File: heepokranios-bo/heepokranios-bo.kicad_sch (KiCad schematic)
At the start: 154 parts, among them J1 Conn_02x02_Odd_Even, J11 PGA_13x13, J14 Conn_02x03_Odd_Even, J15 Conn_02x08_Odd_Even, J16 Conn_02x03_Odd_Even, J17 Conn_02x03_Odd_Even, J2 Conn_02x02_Odd_Even, J21 Conn_01x02, J26 Conn_01x02, J27 Conn_01x02, J29 Conn_01x02, J3 Conn_02x03_Odd_Even, J30 Conn_01x02, J31 Conn_01x02, J32 Conn_01x02, J33 Conn_01x02, J34 Conn_01x02, J35 Conn_01x02, J36 Conn_01x02, J37 Conn_01x02, J38 Conn_01x02, J39 Conn_01x02, J4 Conn_02x03_Odd_Even, J40 Conn_01x02, J41 Conn_01x02, J42 Conn_01x02, J43 Conn_01x02, J48 Conn_01x02, J49 Conn_01x02, J5 Conn_02x03_Odd_Even, J6 Conn_02x04_Odd_Even, J8 Conn_02x03_Odd_Even, J9 Conn_02x02_Odd_Even, SW1 SW_Push, U1 BIWIN_DTS04GE_SMD

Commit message: Routing with extended PGA 13x13 socket
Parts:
- added R9: 330k, Resistor_SMD:R_0603_1608Metric, symbol Device:R_US
- R4: value 10k -> 330
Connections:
- net GND: now also R9.2
- net VREF_EN: now also R9.1
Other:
- note added: "(!) Pulled high from main"
- note added: "(!) VREF_EN added pull-down"
- note removed: "(!) VREF_EN add pull-down. This one is 1.2 V"
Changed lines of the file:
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@@
 	(rectangle
 		(start 105.41 266.7)
-		(end 153.67 290.83)
+		(end 153.67 292.1)
 		(stroke
 			(width 0)
@@
 	)
 	(rectangle
-		(start 105.41 292.1)
+		(start 105.41 293.37)
 		(end 153.67 316.23)
 		(stroke
@@
 	(rectangle
 		(start 160.02 106.68)
-		(end 187.96 128.27)
+		(end 200.66 128.27)
 		(stroke
 			(width 0)
@@
 	(text "VDD for the channel's LNAs"
 		(exclude_from_sim no)
-		(at 129.794 294.132 0)
+		(at 129.794 294.894 0)
 		(effects
 			(font
@@
 		)
 	)
-	(text "(!) VREF_EN add pull-down. This one is 1.2 V"
+	(text "(!) VREF_EN added pull-down"
 		(exclude_from_sim no)
-		(at 167.64 284.48 0)
+		(at 137.668 291.338 0)
 		(effects
 			(font
@@
 		)
 	)
+	(text " (!)\nPulled\nhigh from\nmain"
+		(exclude_from_sim no)
+		(at 194.056 116.586 0)
+		(effects
+			(font
+				(size 1.27 1.27)
+				(color 255 0 32 1)
+			)
+		)
+	)
 	(text "Reference for High (dirty) voltage"
 		(exclude_from_sim no)
@@
 	)
 	(junction
+		(at 186.69 121.92)
+		(diameter 0)
+		(color 0 0 0 0)
+	)
+	(junction
 		(at 436.88 217.17)
 		(diameter 0)
@@
 	)
 	(junction
-		(at 186.69 121.92)
-		(diameter 0)
-		(color 0 0 0 0)
-	)
-	(junction
 		(at 436.88 162.56)
 		(diameter 0)
@@
 	(wire
 		(pts
-			(xy 186.69 121.92) (xy 199.39 121.92)
+			(xy 186.69 121.92) (xy 204.47 121.92)
 		)
 		(stroke
@@
 	(wire
 		(pts
-			(xy 127 289.56) (xy 128.27 289.56)
+			(xy 127 289.56) (xy 137.16 289.56)
 		)
 		(stroke
@@
 	(wire
 		(pts
-			(xy 199.39 156.21) (xy 222.25 156.21)
+			(xy 204.47 156.21) (xy 222.25 156.21)
 		)
 		(stroke
@@
 	(wire
 		(pts
-			(xy 199.39 121.92) (xy 199.39 156.21)
+			(xy 144.78 289.56) (xy 147.32 289.56)
+		)
+		(stroke
+			(width 0)
+			(type default)
+		)
+	)
+	(wire
+		(pts
+			(xy 204.47 121.92) (xy 204.47 156.21)
 		)
 		(stroke
@@
 	(wire
 		(pts
+			(xy 316.23 156.21) (xy 306.07 156.21)
+		)
+		(stroke
+			(width 0)
+			(type default)
+		)
+	)
+	(wire
+		(pts
 			(xy 461.01 162.56) (xy 458.47 162.56)
 		)
@@
 	(wire
 		(pts
+			(xy 314.96 173.99) (xy 306.07 173.99)
+		)
+		(stroke
+			(width 0)
+			(type default)
+		)
+	)
+	(wire
+		(pts
 			(xy 130.81 314.96) (xy 132.08 314.96)
 		)
@@
 	)
 	(label "DMUX_0"
-		(at 306.07 156.21 0)
+		(at 316.23 156.21 0)
 		(effects
 			(font
@@
 	)
 	(label "DMUX_7"
-		(at 306.07 173.99 0)
+		(at 314.96 173.99 0)
 		(effects
 			(font
@@
 			)
 		)
-		(property "Value" "10k"
+		(property "Value" "330"
 			(at 228.6 128.2699 0)
 			(show_name no)
@@
 	)
 	(symbol
+		(lib_id "power:GND")
+		(at 147.32 289.56 90)
+		(unit 1)
+		(body_style 1)
+		(exclude_from_sim no)
+		(in_bom yes)
+		(on_board yes)
+		(in_pos_files yes)
+		(dnp no)
+		(fields_autoplaced yes)
+		(property "Reference" "#PWR0120"
+			(at 153.67 289.56 0)
+			(hide yes)
+			(show_name no)
+			(do_not_autoplace no)
+			(effects
+				(font
+					(size 1.27 1.27)
+				)
+			)
+		)
+		(property "Value" "GND"
+			(at 152.4 289.56 0)
+			(hide yes)
+			(show_name no)
+			(do_not_autoplace no)
+			(effects
+				(font
+					(size 1.27 1.27)
+				)
+			)
+		)
+		(property "Footprint" ""
+			(at 147.32 289.56 0)
+			(hide yes)
+			(show_name no)
+			(do_not_autoplace no)
+			(effects
+				(font
+					(size 1.27 1.27)
+				)
+			)
+		)
+		(property "Datasheet" ""
+			(at 147.32 289.56 0)
+			(hide yes)
+			(show_name no)
+			(do_not_autoplace no)
+			(effects
+				(font
+					(size 1.27 1.27)
+				)
+			)
+		)
+		(property "Description" "Power symbol creates a global label with name \"GND\" , ground"
+			(at 147.32 289.56 0)
+			(hide yes)
+			(show_name no)
+			(do_not_autoplace no)
+			(effects
+				(font
+					(size 1.27 1.27)
+				)
+			)
+		)
+		(pin "1"
+		)
+		(instances
+			(project "heepokranios-bo"
+				(path "/ee6a4f3e-c170-41be-a165-91e3bf2c65c5"
+					(reference "#PWR0120")
+					(unit 1)
+				)
+			)
+		)
+	)
+	(symbol
 		(lib_id "heepokranios-bo-library:SMA_w_tp")
 		(at 208.28 311.15 270)
@@
 					(unit 1)
 				)
+			)
+		)
+	)
+	(symbol
+		(lib_id "Device:R_US")
+		(at 140.97 289.56 90)
+		(unit 1)
+		(body_style 1)
+		(exclude_from_sim no)
+		(in_bom yes)
+		(on_board yes)
+		(in_pos_files yes)
+		(dnp no)
+		(property "Reference" "R9"
+			(at 140.716 284.48 90)
+			(show_name no)
+			(do_not_autoplace no)
+			(effects
+				(font
+					(size 1.27 1.27)
+				)
+			)
+		)
+		(property "Value" "330k"
+			(at 140.97 286.766 90)
+			(show_name no)
+			(do_not_autoplace no)
+			(effects
+				(font
+					(size 1.27 1.27)
+				)
+			)
+		)
+		(property "Footprint" "Resistor_SMD:R_0603_1608Metric"
+			(at 141.224 288.544 90)
+			(hide yes)
+			(show_name no)
+			(do_not_autoplace no)
+			(effects
+				(font
+					(size 1.27 1.27)
+				)
+			)
+		)
+		(property "Datasheet" ""
+			(at 140.97 289.56 0)
+			(hide yes)
+			(show_name no)
+			(do_not_autoplace no)
+			(effects
+				(font
+					(size 1.27 1.27)
+				)
+			)
+		)
+		(property "Description" "Resistor, US symbol"
+			(at 140.97 289.56 0)
+			(hide yes)
+			(show_name no)
+			(do_not_autoplace no)
+			(effects
+				(font
+					(size 1.27 1.27)
+				)
+			)
+		)
+		(pin "2"
+		)
+		(pin "1"
+		)
+		(instances
+			(project "heepokranios-bo"
+				(path "/ee6a4f3e-c170-41be-a165-91e3bf2c65c5"
+					(reference "R9")
+					(unit 1)
+				)

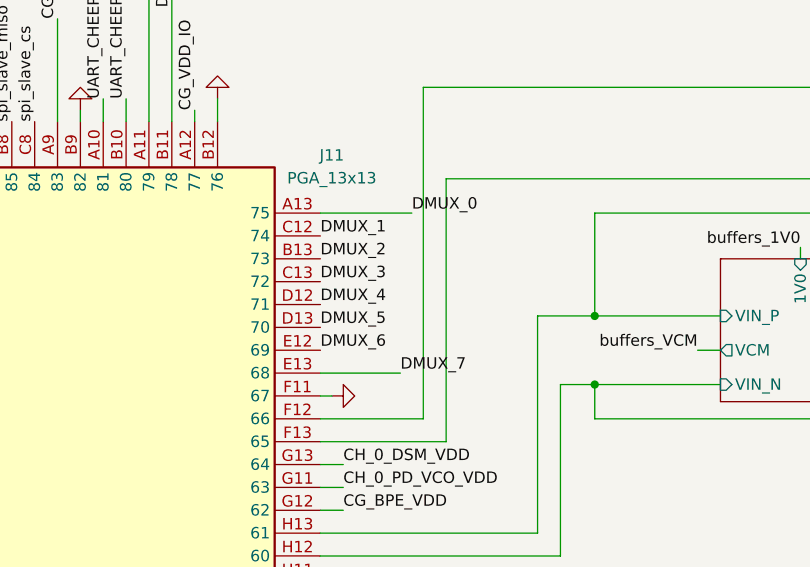
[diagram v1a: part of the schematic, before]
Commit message: Re-routed dMUX 0-7 pins from chip as they were inverted
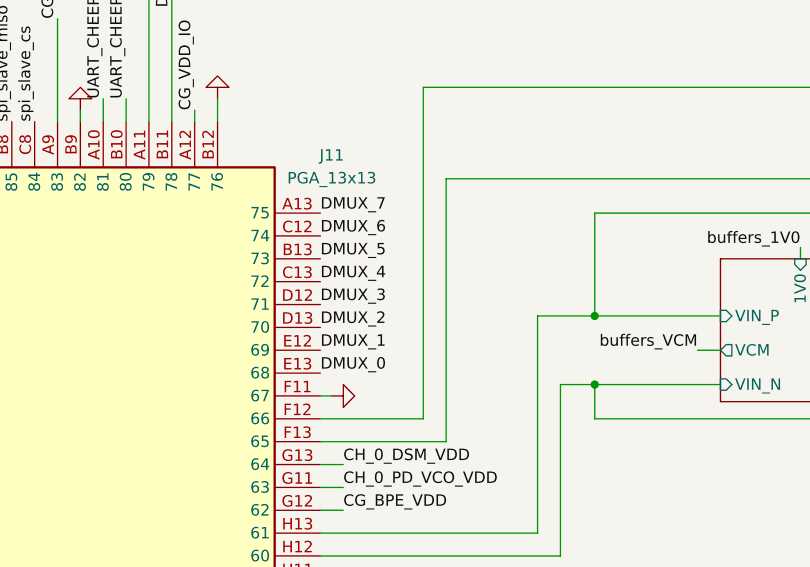
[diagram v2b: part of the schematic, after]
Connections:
- net DMUX_0: now also J11.E13 (68); no longer J11.A13 (75)
- net DMUX_1: now also J11.E12 (69); no longer J11.C12 (74)
- net DMUX_2: now also J11.D13 (70); no longer J11.B13 (73)
- net DMUX_3: now also J11.D12 (71); no longer J11.C13 (72)
- net DMUX_4: now also J11.C13 (72); no longer J11.D12 (71)
- net DMUX_5: now also J11.B13 (73); no longer J11.D13 (70)
- net DMUX_6: now also J11.C12 (74); no longer J11.E12 (69)
- net DMUX_7: now also J11.A13 (75); no longer J11.E13 (68)
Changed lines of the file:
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@@
 	(wire
 		(pts
-			(xy 316.23 156.21) (xy 306.07 156.21)
-		)
-		(stroke
-			(width 0)
-			(type default)
-		)
-	)
-	(wire
-		(pts
 			(xy 461.01 162.56) (xy 458.47 162.56)
 		)
@@
 	(wire
 		(pts
-			(xy 314.96 173.99) (xy 306.07 173.99)
-		)
-		(stroke
-			(width 0)
-			(type default)
-		)
-	)
-	(wire
-		(pts
 			(xy 130.81 314.96) (xy 132.08 314.96)
 		)
@@
 		)
 	)
-	(label "DMUX_2"
+	(label "DMUX_5"
 		(at 306.07 161.29 0)
 		(effects
@@
 		)
 	)
-	(label "DMUX_0"
-		(at 316.23 156.21 0)
+	(label "DMUX_7"
+		(at 306.07 156.21 0)
 		(effects
 			(font
@@
 		)
 	)
-	(label "DMUX_7"
-		(at 314.96 173.99 0)
+	(label "DMUX_0"
+		(at 306.07 173.99 0)
 		(effects
 			(font
@@
 		)
 	)
-	(label "DMUX_6"
+	(label "DMUX_1"
 		(at 306.07 171.45 0)
 		(effects
@@
 		)
 	)
-	(label "DMUX_5"
+	(label "DMUX_2"
 		(at 306.07 168.91 0)
 		(effects
@@
 		)
 	)
-	(label "DMUX_1"
+	(label "DMUX_6"
 		(at 306.07 158.75 0)
 		(effects
@@
 		)
 	)
-	(label "DMUX_3"
+	(label "DMUX_4"
 		(at 306.07 163.83 0)
 		(effects
@@
 		)
 	)
-	(label "DMUX_4"
+	(label "DMUX_3"
 		(at 306.07 166.37 0)
 		(effects
